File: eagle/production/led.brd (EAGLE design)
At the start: 47 x 82 mm, 12 parts, among them Q1 TIP120, Q2 TIP120, Q3 TIP120, U1 ATMEGA328P_PDIP

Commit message: [Eagle] Board repaired
Signed-off-by: Roman3349 <ondracek.roman@centrum.cz>
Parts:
- moved SV1 7.73 mm to (32.5, 47.7), turned to 180 degrees
- moved R1 7.62 mm to (19.7, 56.6)
- moved IC1 7.07 mm to (6.52, 58.9)
- moved Q3 6.20 mm to (39.0, 17.6), turned to 180 degrees
- moved Q1 5.84 mm to (10.4, 17.7), turned to 180 degrees
- moved Q2 5.61 mm to (23.8, 17.7), turned to 180 degrees
- moved X2 4.12 mm to (28.6, 10.9)
- moved D1 1.41 mm to (11.1, 63.3)
- moved U1 1.00 mm to (27.2, 33.0)
- moved SV2 0.41 mm to (38.5, 57.8)
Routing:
- net +5V: track 128.1 -> 60.7 mm
- net N$6: track 80.3 -> 25.6 mm
- net N$5: track 59.7 -> 77.3 mm
- net N$7: track 29.1 -> 12.4 mm
- net N$2: track 35.6 -> 22.7 mm
- net N$8: track 36.9 -> 26.3 mm
- net N$14: track 49.7 -> 43.0 mm
- net N$13: track 19.0 -> 12.6 mm
- net N$12: track 19.6 -> 14.0 mm
- net N$1: track 16.7 -> 12.9 mm
- net N$11: track 7.87 -> 10.4 mm
- net N$10: track 19.7 -> 21.2 mm
- net +12V: track 66.5 -> 67.7 mm
- net N$3: track 19.9 -> 20.4 mm

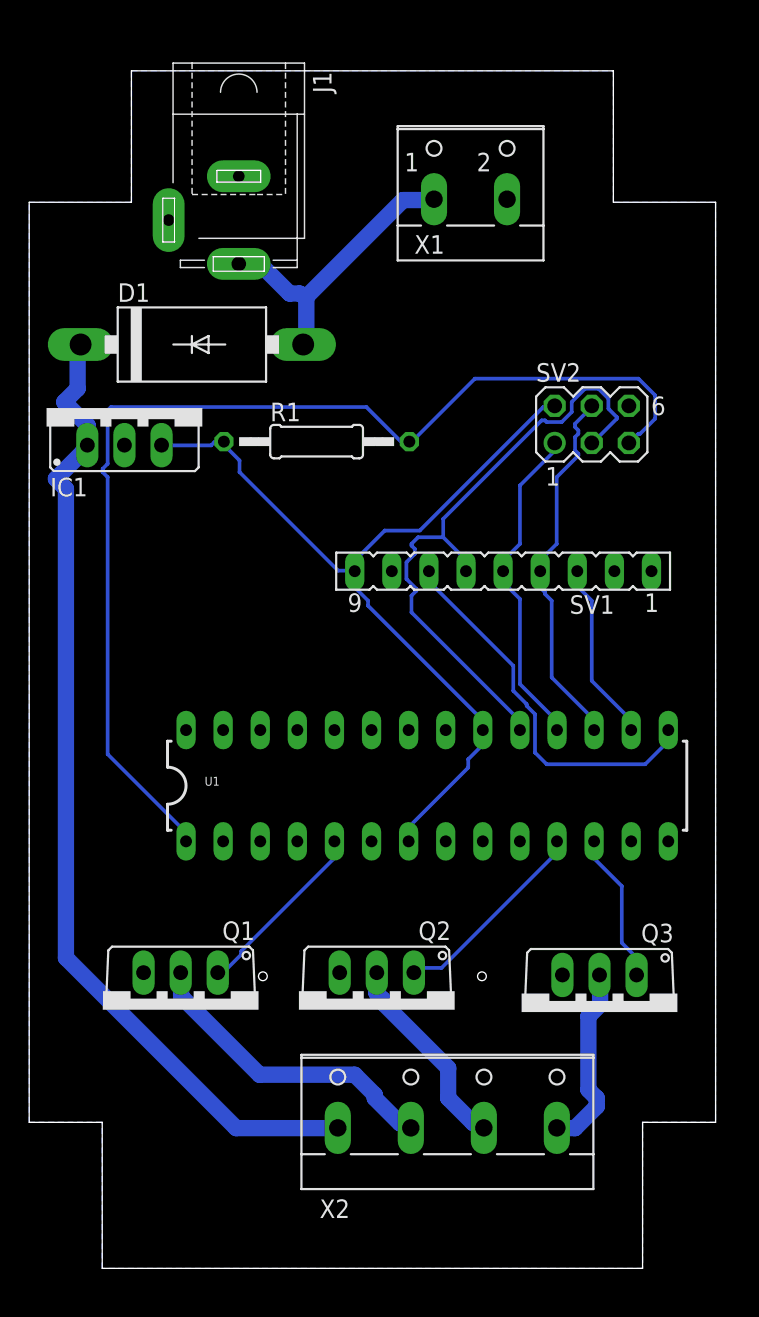
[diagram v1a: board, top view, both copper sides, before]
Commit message: [Eagle] Edited schema and board
Signed-off-by: Roman3349 <ondracek.roman@centrum.cz>
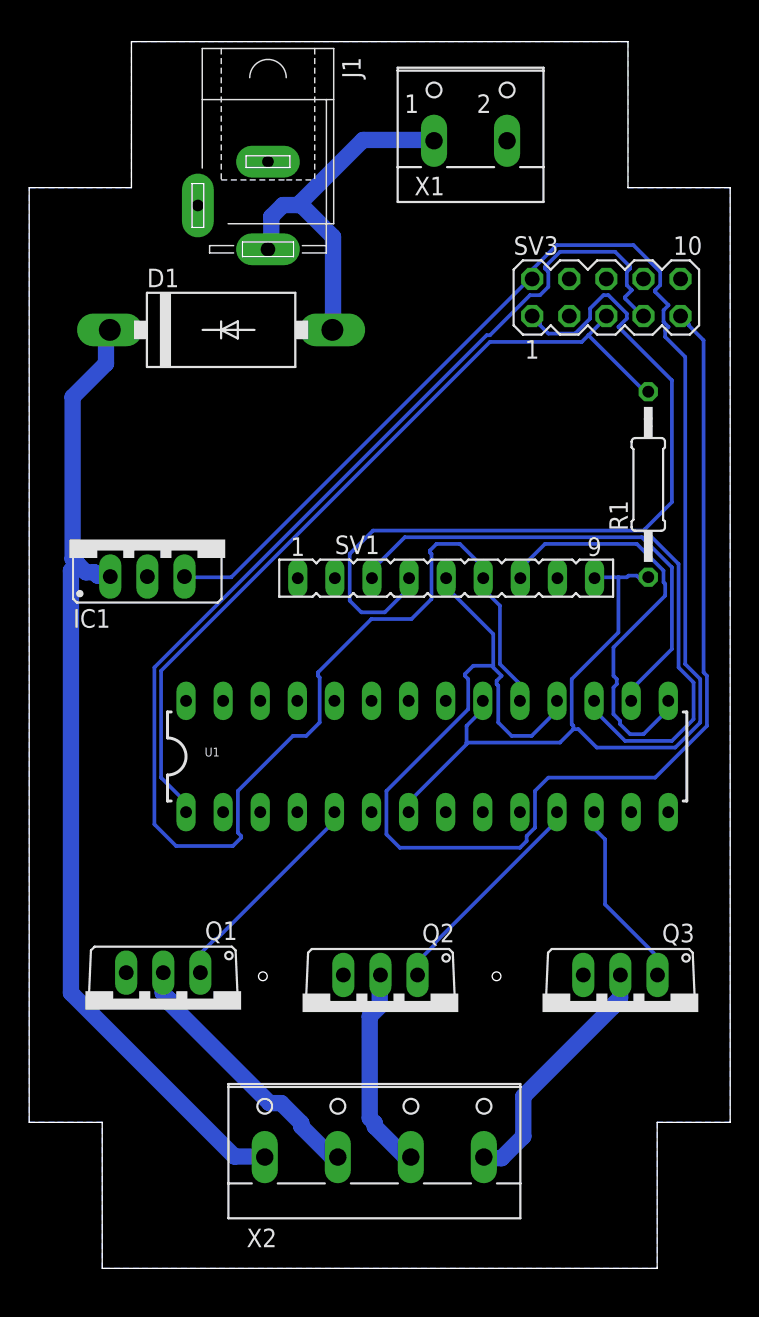
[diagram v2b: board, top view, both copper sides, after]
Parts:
- removed SV2: (no value), con-lstb:MA03-2
- added SV3: (no value), con-lstb:MA05-2
- moved R1 22.9 mm to (42.4, 53.7), turned to 90 degrees
- moved IC1 9.14 mm to (8.09, 49.9)
- moved X2 5.39 mm to (23.6, 8.89)
- moved X1 4.00 mm to (30.2, 78.5)
- moved SV1 3.93 mm to (28.6, 47.3), turned to 0 degrees
- moved D1 2.24 mm to (13.1, 64.3)
- moved J1 2.24 mm to (16.4, 72.8)
- moved U1 2.00 mm to (27.2, 35.0)
- moved Q3 1.43 mm to (40.5, 17.6)
- moved Q1 1.19 mm to (9.18, 17.7)
- moved Q2 0.30 mm to (24.1, 17.6)
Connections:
- net +5V: now also SV3.2; no longer SV2.2
- net GND: now also SV3.10, SV3.4; no longer SV2.6
- net N$14: now also SV3.7; no longer SV2.3
- net N$2: now also SV3.9; no longer SV2.1
- net N$5: now also SV3.5; no longer SV2.5
- net N$6: now also SV3.1; no longer SV2.4
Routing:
- net N$14: track 43.0 -> 110.1 mm
- net N$2: track 22.7 -> 89.3 mm
- net +5V: track 60.7 -> 118.9 mm
- net N$6: track 25.6 -> 79.5 mm
- net N$7: track 12.4 -> 33.2 mm
- net N$5: track 77.3 -> 56.7 mm
- net N$3: track 20.4 -> 25.3 mm
- net N$1: track 12.9 -> 17.2 mm
- net N$10: track 21.2 -> 18.3 mm
- net N$8: track 26.3 -> 29.2 mm
- net N$11: track 10.4 -> 13.0 mm
- net N$13: track 12.6 -> 14.9 mm
- net N$12: track 14.0 -> 15.1 mm
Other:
- board size 47 x 82 mm -> 48 x 84 mm

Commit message: [Eagle] Update board
Signed-off-by: Roman3349 <ondracek.roman@centrum.cz>
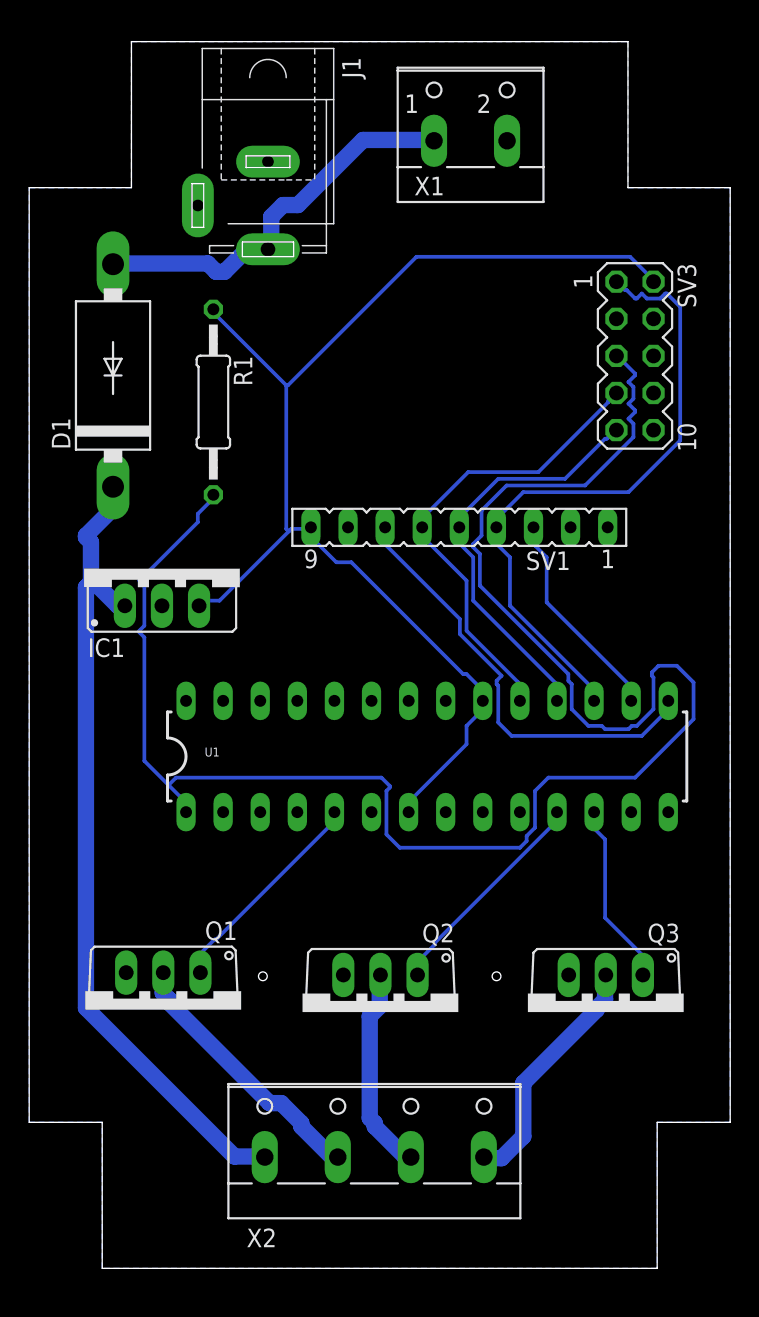
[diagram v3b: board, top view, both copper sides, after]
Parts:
- moved R1 30.3 mm to (12.6, 59.3), turned to 270 degrees
- moved D1 8.03 mm to (5.74, 61.1), turned to 90 degrees
- moved SV3 4.45 mm to (41.5, 62.5), turned to 270 degrees
- moved SV1 3.59 mm to (29.4, 50.7), turned to 180 degrees
- moved IC1 2.24 mm to (9.09, 47.9)
- moved Q3 1.00 mm to (39.5, 17.6)
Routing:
- net N$14: track 110.1 -> 32.3 mm
- net N$5: track 56.7 -> 122.8 mm
- net N$2: track 89.3 -> 28.6 mm
- net +5V: track 118.9 -> 84.1 mm
- net N$6: track 79.5 -> 44.8 mm
- net N$7: track 33.2 -> 14.7 mm
- net +12V: track 67.3 -> 56.2 mm
- net N$3: track 25.3 -> 27.2 mm
- net N$8: track 29.2 -> 30.2 mm

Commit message: [Eagle] Added capacitors and resistors
Signed-off-by: Roman3349 <ondracek.roman@centrum.cz>
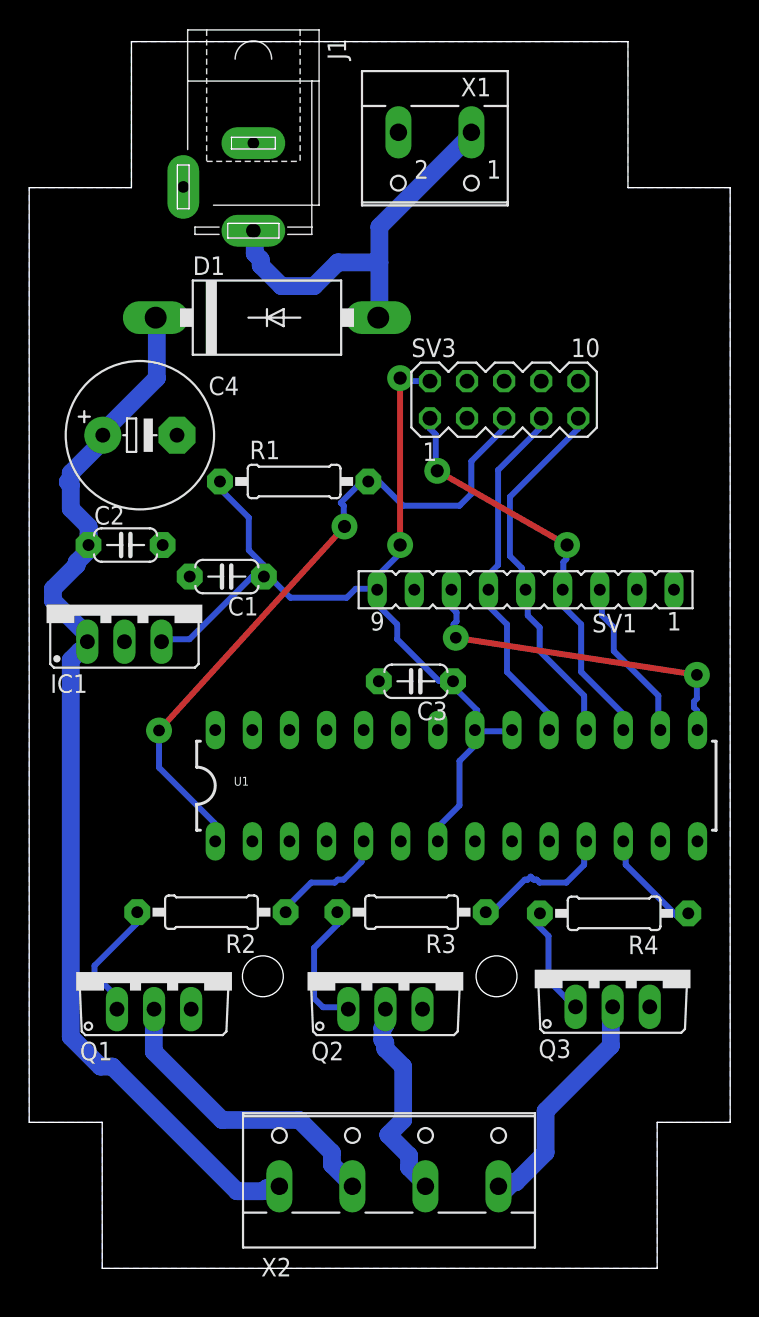
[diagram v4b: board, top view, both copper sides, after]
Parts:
- added C1, C3: 100n, rcl:C050-024X044
- added C2: 330n, rcl:C050-024X044
- added C4: 680u, rcl:E5-10,5
- added R2, R3, R4: 1k, rcl:0207/10
- R1: device resistor:0207/12 -> resistor:0207/10
- moved D1 11.3 mm to (16.3, 65.1), turned to 0 degrees
- moved SV3 9.45 mm to (32.5, 59.5), turned to 0 degrees
- moved R1 7.76 mm to (18.1, 53.9), turned to 0 degrees
- moved SV1 6.23 mm to (34.0, 46.5)
- moved IC1 3.56 mm to (6.52, 45.5)
- moved X1 3.13 mm to (27.8, 76.5), turned to 180 degrees
- moved Q3 2.94 mm to (40.0, 20.4), turned to 0 degrees
- moved U1 2.83 mm to (29.2, 33.0)
- moved Q2 2.76 mm to (24.4, 20.3), turned to 0 degrees
- moved Q1 2.66 mm to (8.55, 20.3), turned to 0 degrees
- moved X2 2.24 mm to (24.6, 6.89)
- moved J1 1.62 mm to (15.3, 74.0)
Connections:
- new net N$15: Q2.B, R3.2
- new net N$16: Q3.B, R4.2
- new net N$4: Q1.B, R2.2
- net +12V: now also C2.1, C4.+
- net +5V: now also C1.1, C3.1, U1.21
- net GND: now also C1.2, C2.2, C3.2, C4.-
- net N$11: now also R4.1; no longer Q3.B
- net N$12: now also R3.1; no longer Q2.B
- net N$13: now also R2.1; no longer Q1.B
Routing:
- net N$5: track 122.8 -> 46.5 mm, vias 0 -> 2
- net +12V: track 56.2 -> 74.4 mm
- net +5V: track 84.1 -> 67.0 mm, vias 0 -> 2
- net N$6: track 44.8 -> 28.5 mm, vias 0 -> 2
- net N$15: track 0.00 -> 9.26 mm
- net N$4: track 0.00 -> 8.53 mm
- net N$14: track 32.3 -> 24.5 mm
- net N$16: track 0.00 -> 7.70 mm
- net N$13: track 14.9 -> 8.29 mm
- net N$8: track 30.2 -> 24.3 mm, vias 0 -> 2
- net N$11: track 12.6 -> 7.50 mm
- net N$12: track 15.1 -> 10.2 mm
- net N$7: track 14.7 -> 11.3 mm
- net N$2: track 28.6 -> 25.5 mm
- net N$10: track 18.3 -> 20.9 mm
